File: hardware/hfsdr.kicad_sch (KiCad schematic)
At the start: 25 parts, among them J1 USB_C_Receptacle_USB2.0_16P, SW1 RST, SW2 BOOT0, U3 CH32V30xRxTx

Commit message: layout + some routing
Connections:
- net +3.3V: now also SW1.1 (A); no longer R4.1, SW1.2 (B)
- net SWDIO: now reaches U3.46 (SWDIO)
- net SWCLK: now reaches U3.49 (SWCLK)
- net at C20.2: now also R4.1, SW1.2 (B); no longer SW1.1 (A)
- no-connect marks 0 -> 4
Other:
- moved on the sheet: C20, SW1

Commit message: feat: routing
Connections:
- net DM renamed DN
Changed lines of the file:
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@@
 		)
 	)
-	(global_label "DM"
+	(global_label "DN"
 		(shape input)
 		(at 124.46 119.38 180)
@@
 		)
 		(property "Intersheetrefs" "${INTERSHEET_REFS}"
-			(at 118.7534 119.38 0)
+			(at 118.8743 119.38 0)
 			(effects
 				(font
@@
 		)
 	)
-	(global_label "DM"
+	(global_label "DN"
 		(shape input)
 		(at 241.3 43.18 180)
@@
 		)
 		(property "Intersheetrefs" "${INTERSHEET_REFS}"
-			(at 235.5934 43.18 0)
-			(effects
-				(font
+			(at 235.7143 43.18 0)
+			(effects
+				(font

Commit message: feat: most rules fixed?
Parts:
- removed H1: MountingHole_Pad, MountingHole:MountingHole_3.2mm_M3_Pad, symbol Mechanical:MountingHole_Pad
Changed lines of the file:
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@@
-	)
-	(symbol
-		(lib_id "Mechanical:MountingHole_Pad")
-		(at 222.25 76.2 0)
-		(unit 1)
-		(exclude_from_sim yes)
-		(in_bom no)
-		(on_board yes)
-		(dnp no)
-		(fields_autoplaced yes)
-		(property "Reference" "H1"
-			(at 224.79 73.6599 0)
-			(effects
-				(font
-					(size 1.27 1.27)
-				)
-				(justify left)
-			)
-		)
-		(property "Value" "MountingHole_Pad"
-			(at 224.79 76.1999 0)
-			(effects
-				(font
-					(size 1.27 1.27)
-				)
-				(justify left)
-			)
-		)
-		(property "Footprint" "MountingHole:MountingHole_3.2mm_M3_Pad"
-			(at 222.25 76.2 0)
-			(effects
-				(font
-					(size 1.27 1.27)
-				)
-				(hide yes)
-			)
-		)
-		(property "Datasheet" "~"
-			(at 222.25 76.2 0)
-			(effects
-				(font
-					(size 1.27 1.27)
-				)
-				(hide yes)
-			)
-		)
-		(property "Description" "Mounting Hole with connection"
-			(at 222.25 76.2 0)
-			(effects
-				(font
-					(size 1.27 1.27)
-				)
-				(hide yes)
-			)
-		)
-		(pin "1"
-		)
-		(instances
-			(project ""
-				(path "/a11445ed-c3bd-4d1c-a039-1c09b0dceab8"
-					(reference "H1")
-					(unit 1)
-				)
-			)
-		)
 	)
 	(symbol

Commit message: feat: hfsdr rough
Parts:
- added R12, R13, R14: 10k, Resistor_SMD:R_0805_2012Metric_Pad1.20x1.40mm_HandSolder, symbol Device:R
- added R15, R16: 4.7k, Resistor_SMD:R_0805_2012Metric_Pad1.20x1.40mm_HandSolder, symbol Device:R
- added SW4: EC12E2430803, easyeda2kicad:SW-TH_EC12EXXXX, symbol easyeda2kicad:EC12E2430803
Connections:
- net +3.3V: now also FPC1.17, R12.2, R13.2, R14.2, R15.2, R16.2
- net CS: now also U3.54 (PD2)
- net GND: now also SW4.C, SW4.D
- net RS: now also U3.53 (PC12)
- net RST: now also C20.2, FPC1.15, R4.1, SW1.2 (B)
- net SCL: now also FPC1.13, R15.1
- net SDA: now also FPC1.14, R16.1
- net ENC_B: now reaches U3.2 (PC13)
- net ENC_B: now also R14.1, SW4.B
- net ENC_A: now reaches U3.3 (PC14)
- net ENC_A: now also R13.1, SW4.A
- net ENC_BTN: now reaches U3.4 (PC15)
- net ENC_BTN: now also R12.1, SW4.E
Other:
- note added: "Touchscreen"

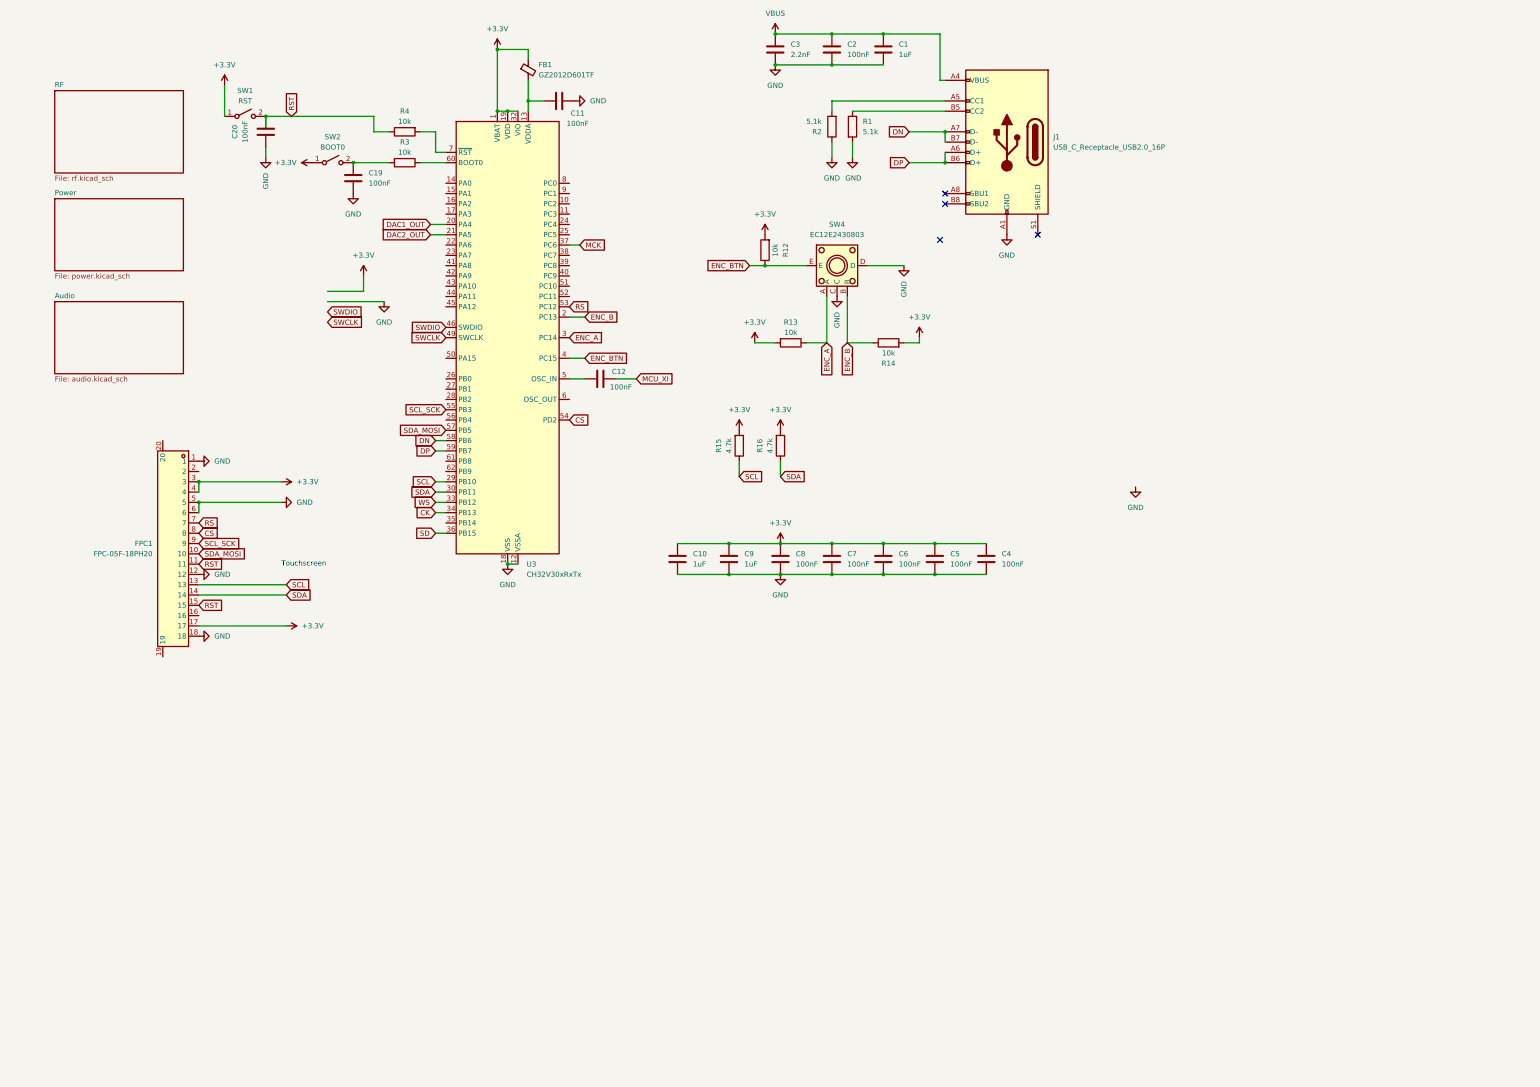
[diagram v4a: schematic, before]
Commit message: feat: add pads + fix adc chip footprint
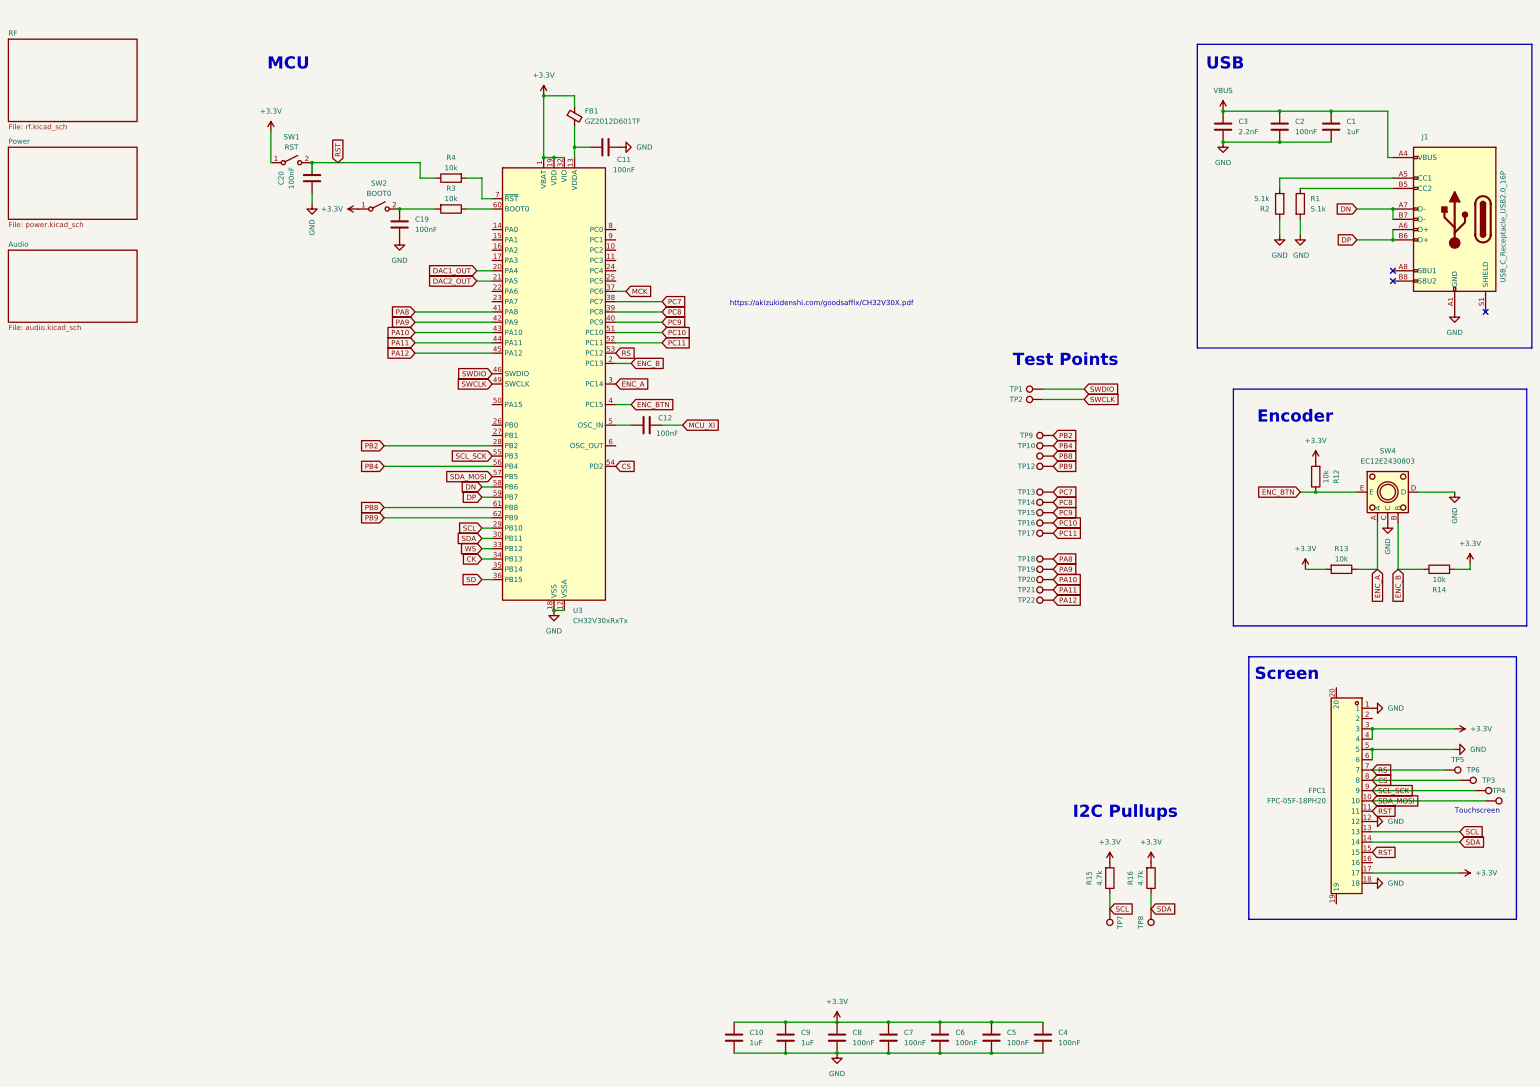
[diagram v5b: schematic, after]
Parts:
- added TP1, TP10, TP11, TP12, TP13, TP14, TP15, TP16, TP17, TP18, TP19, TP2, TP20, TP21, TP22, TP3, TP4, TP5, TP6, TP7, TP8, TP9: TestPoint, TestPoint:TestPoint_Pad_1.0x1.0mm, symbol Connector:TestPoint
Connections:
- net CS: now also TP6.1
- net RS: now also TP5.1
- net SCL: now also TP7.1
- net SCL_SCK: now also TP3.1
- net SDA: now also TP8.1
- net SDA_MOSI: now also TP4.1
- net SWCLK: now also TP2.1
- net SWDIO: now also TP1.1
- net PB2: now reaches U3.28 (PB2)
- net PB2: now also TP9.1
- net PC7: now reaches U3.38 (PC7)
- net PC7: now also TP13.1
- net PC8: now reaches U3.39 (PC8)
- net PC8: now also TP14.1
- net PC9: now reaches U3.40 (PC9)
- net PC9: now also TP15.1
- net PA8: now reaches U3.41 (PA8)
- net PA8: now also TP18.1
- net PA9: now reaches U3.42 (PA9)
- net PA9: now also TP19.1
- net PA10: now reaches U3.43 (PA10)
- net PA10: now also TP20.1
- net PA11: now reaches U3.44 (PA11)
- net PA11: now also TP21.1
- net PA12: now reaches U3.45 (PA12)
- net PA12: now also TP22.1
- net PC10: now reaches U3.51 (PC10)
- net PC10: now also TP16.1
- net PC11: now reaches U3.52 (PC11)
- net PC11: now also TP17.1
- net PB4: now reaches U3.56 (PB4)
- net PB4: now also TP10.1
- net PB8: now reaches U3.61 (PB8)
- net PB8: now also TP11.1
- net PB9: now reaches U3.62 (PB9)
- net PB9: now also TP12.1
- no-connect marks 4 -> 3
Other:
- note added: "Encoder"
- note added: "I2C Pullups"
- note added: "MCU"
- note added: "Screen"
- note added: "Test Points"
- note added: "USB"
- note added: "https://akizukidenshi.com/goodsaffix/CH32V30X.pdf"
- moved on the sheet: C1, C10, C11, C12, C19, C2, C20, C3, C4, C5, C6, C7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

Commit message: feat: add front LEDs
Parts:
- added D3, D4: LED, LED_SMD:LED_0603_1608Metric_Pad1.05x0.95mm_HandSolder, symbol Device:LED
- added R17, R18: 470, Resistor_SMD:R_0603_1608Metric_Pad0.98x0.95mm_HandSolder, symbol Device:R
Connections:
- net GND: now also R17.2, R18.2
- net LED1: now reaches U3.8 (PC0)
- net LED1: now also D3.2 (A)
- net LED2: now reaches U3.9 (PC1)
- net LED2: now also D4.2 (A)
- new net: D3.1 (K), R17.1
- new net: D4.1 (K), R18.1

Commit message: Production ready
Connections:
- net BATT_ADC: now reaches U3.24 (PC4)
- net VBUS_ADC: now reaches U3.25 (PC5)
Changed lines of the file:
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@@
+		)
+	)
+	(global_label "BATT_ADC"
+		(shape input)
+		(at 168.91 77.47 0)
+		(fields_autoplaced yes)
+		(effects
+			(font
+				(size 1.27 1.27)
+			)
+			(justify left)
+		)
+		(property "Intersheetrefs" "${INTERSHEET_REFS}"
+			(at 180.7852 77.47 0)
+			(effects
+				(font
+					(size 1.27 1.27)
+				)
+				(justify left)
+				(hide yes)
+			)
 		)
 	)
@@
 		)
 	)
+	(global_label "BATT_ADC"
+		(shape input)
+		(at 187.96 143.51 0)
+		(fields_autoplaced yes)
+		(effects
+			(font
+				(size 1.27 1.27)
+			)
+			(justify left)
+		)
+		(property "Intersheetrefs" "${INTERSHEET_REFS}"
+			(at 199.8352 143.51 0)
+			(effects
+				(font
+					(size 1.27 1.27)
+				)
+				(justify left)
+				(hide yes)
+			)
+		)
+	)
 	(global_label "LED1"
 		(shape input)
@@
 				(hide yes)
 			)
+		)
+	)
+	(global_label "VBUS_ADC"
+		(shape input)
+		(at 168.91 80.01 0)
+		(fields_autoplaced yes)
+		(effects
+			(font
+				(size 1.27 1.27)
+			)
+			(justify left)
+		)
+		(property "Intersheetrefs" "${INTERSHEET_REFS}"
+			(at 181.39 80.01 0)
+			(effects
+				(font
+					(size 1.27 1.27)
+				)
+				(justify left)
+				(hide yes)
+			)

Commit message: Update hardware
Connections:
- net +3.3V: now also C20.2, R4.1, SW1.2 (B); no longer SW1.1 (A)
- net GND: now also R3.2, SW1.1 (A)
- net PC10: now also FPC1.15
- net PC11: now also FPC1.11
- net at C19.1, SW2.2 (B): now also R3.1, U3.60 (BOOT0); no longer R3.2
- removed net RST: C20.2, FPC1.11, FPC1.15, R4.1, SW1.2 (B)
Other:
- moved on the sheet: R3, SW1
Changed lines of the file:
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@@
 	)
 	(junction
+		(at 128.27 62.23)
+		(diameter 0)
+		(color 0 0 0 0)
+	)
+	(junction
+		(at 115.57 62.23)
+		(diameter 0)
+		(color 0 0 0 0)
+	)
+	(junction
 		(at 236.22 270.51)
 		(diameter 0)
@@
 	)
 	(junction
-		(at 115.57 62.23)
+		(at 93.98 60.96)
 		(diameter 0)
 		(color 0 0 0 0)
@@
 	)
 	(junction
+		(at 191.77 92.71)
+		(diameter 0)
+		(color 0 0 0 0)
+	)
+	(junction
+		(at 115.57 69.85)
+		(diameter 0)
+		(color 0 0 0 0)
+	)
+	(junction
 		(at 318.77 45.72)
 		(diameter 0)
@@
 	)
 	(junction
+		(at 179.07 95.25)
+		(diameter 0)
+		(color 0 0 0 0)
+	)
+	(junction
 		(at 360.68 62.23)
 		(diameter 0)
@@
 	(wire
 		(pts
-			(xy 83.82 43.18) (xy 83.82 50.8)
+			(xy 119.38 87.63) (xy 138.43 87.63)
 		)
 		(stroke
@@
 	(wire
 		(pts
-			(xy 119.38 87.63) (xy 138.43 87.63)
+			(xy 318.77 38.1) (xy 332.74 38.1)
 		)
 		(stroke
@@
 	(wire
 		(pts
-			(xy 318.77 38.1) (xy 332.74 38.1)
+			(xy 332.74 54.61) (xy 360.68 54.61)
 		)
 		(stroke
@@
 	(wire
 		(pts
-			(xy 332.74 54.61) (xy 360.68 54.61)
+			(xy 339.09 151.13) (xy 344.17 151.13)
 		)
 		(stroke
@@
 	(wire
 		(pts
-			(xy 339.09 151.13) (xy 344.17 151.13)
+			(xy 135.89 130.81) (xy 138.43 130.81)
 		)
 		(stroke
@@
 	(wire
 		(pts
-			(xy 135.89 130.81) (xy 138.43 130.81)
+			(xy 360.68 67.31) (xy 360.68 69.85)
 		)
 		(stroke
@@
 	(wire
 		(pts
-			(xy 360.68 67.31) (xy 360.68 69.85)
+			(xy 82.55 60.96) (xy 93.98 60.96)
 		)
 		(stroke
@@
 	(wire
 		(pts
-			(xy 115.57 62.23) (xy 124.46 62.23)
+			(xy 179.07 95.25) (xy 168.91 95.25)
 		)
 		(stroke
@@
 	(wire
 		(pts
+			(xy 198.12 95.25) (xy 191.77 95.25)
+		)
+		(stroke
+			(width 0)
+			(type default)
+		)
+	)
+	(wire
+		(pts
+			(xy 191.77 92.71) (xy 168.91 92.71)
+		)
+		(stroke
+			(width 0)
+			(type default)
+		)
+	)
+	(wire
+		(pts
 			(xy 248.92 270.51) (xy 261.62 270.51)
 		)
@@
 	(wire
 		(pts
+			(xy 93.98 43.18) (xy 93.98 50.8)
+		)
+		(stroke
+			(width 0)
+			(type default)
+		)
+	)
+	(wire
+		(pts
+			(xy 115.57 69.85) (xy 128.27 69.85)
+		)
+		(stroke
+			(width 0)
+			(type default)
+		)
+	)
+	(wire
+		(pts
 			(xy 377.19 203.2) (xy 355.6 203.2)
 		)
@@
 	(wire
 		(pts
-			(xy 180.34 92.71) (xy 168.91 92.71)
+			(xy 82.55 50.8) (xy 93.98 50.8)
+		)
+		(stroke
+			(width 0)
+			(type default)
+		)
+	)
+	(wire
+		(pts
+			(xy 195.58 92.71) (xy 191.77 92.71)
 		)
 		(stroke
@@
 	(wire
 		(pts
+			(xy 191.77 95.25) (xy 191.77 92.71)
+		)
+		(stroke
+			(width 0)
+			(type default)
+		)
+	)
+	(wire
+		(pts
 			(xy 180.34 115.57) (xy 185.42 115.57)
 		)
@@
 	(wire
 		(pts
+			(xy 115.57 62.23) (xy 128.27 62.23)
+		)
+		(stroke
+			(width 0)
+			(type default)
+		)
+	)
+	(wire
+		(pts
 			(xy 180.34 87.63) (xy 168.91 87.63)
 		)
@@
 	(wire
 		(pts
+			(xy 182.88 97.79) (xy 179.07 97.79)
+		)
+		(stroke
+			(width 0)
+			(type default)
+		)
+	)
+	(wire
+		(pts
 			(xy 381 205.74) (xy 355.6 205.74)
 		)
@@
 	(wire
 		(pts
-			(xy 180.34 95.25) (xy 168.91 95.25)
+			(xy 180.34 95.25) (xy 179.07 95.25)
 		)
 		(stroke
@@
 	(wire
 		(pts
+			(xy 179.07 97.79) (xy 179.07 95.25)
+		)
+		(stroke
+			(width 0)
+			(type default)
+		)
+	)
+	(wire
+		(pts
 			(xy 158.75 41.91) (xy 158.75 46.99)
 		)
@@
 	(wire
 		(pts
-			(xy 132.08 62.23) (xy 138.43 62.23)
+			(xy 128.27 62.23) (xy 138.43 62.23)
 		)
 		(stroke
@@
 		)
 	)
-	(global_label "RST"
-		(shape input)
-		(at 100.33 50.8 90)
-		(fields_autoplaced yes)
-		(effects
-			(font
-				(size 1.27 1.27)
-			)
-			(justify left)
-		)
-		(property "Intersheetrefs" "${INTERSHEET_REFS}"
-			(at 100.33 44.3677 90)
-			(effects
-				(font
-					(size 1.27 1.27)
-				)
-				(justify left)
-				(hide yes)
-			)
-		)
-	)
 	(global_label "PB8"
 		(shape input)
@@
 		)
 	)
+	(global_label "RST"
+		(shape input)
+		(at 182.88 97.79 0)
+		(fields_autoplaced yes)
+		(effects
+			(font
+				(size 1.27 1.27)
+			)
+			(justify left)
+		)
+		(property "Intersheetrefs" "${INTERSHEET_REFS}"
+			(at 189.3123 97.79 0)
+			(effects
+				(font
+					(size 1.27 1.27)
+				)
+				(justify left)
+				(hide yes)
+			)
+		)
+	)
+	(global_label "TP_RST"
+		(shape input)
+		(at 198.12 95.25 0)
+		(fields_autoplaced yes)
+		(effects
+			(font
+				(size 1.27 1.27)
+			)
+			(justify left)
+		)
+		(property "Intersheetrefs" "${INTERSHEET_REFS}"
+			(at 207.7575 95.25 0)
+			(effects
+				(font
+					(size 1.27 1.27)
+				)
+				(justify left)
+				(hide yes)
+			)
+		)
+	)
 	(global_label "VBUS_ADC"
 		(shape input)
@@
 		)
 	)
-	(global_label "RST"
+	(global_label "TP_RST"
 		(shape input)
 		(at 355.6 220.98 0)
@@
 		)
 		(property "Intersheetrefs" "${INTERSHEET_REFS}"
-			(at 362.0323 220.98 0)
+			(at 365.2375 220.98 0)
 			(effects
 				(font
@@
 	(global_label "PC10"
 		(shape input)
-		(at 180.34 92.71 0)
+		(at 195.58 92.71 0)
 		(fields_autoplaced yes)
 		(effects
@@
 		)
 		(property "Intersheetrefs" "${INTERSHEET_REFS}"
-			(at 188.2842 92.71 0)
+			(at 203.5242 92.71 0)
 			(effects
 				(font
@@
 	(symbol
 		(lib_id "power:+3.3V")
-		(at 83.82 43.18 0)
+		(at 93.98 43.18 0)
 		(unit 1)
 		(exclude_from_sim no)
@@
 		(fields_autoplaced yes)
 		(property "Reference" "#PWR025"
-			(at 83.82 46.99 0)
+			(at 93.98 46.99 0)
 			(effects
 				(font
@@
 		)
 		(property "Value" "+3.3V"
-			(at 83.82 38.1 0)
+			(at 93.98 38.1 0)
 			(effects
 				(font
@@
 		)
 		(property "Footprint" ""
-			(at 83.82 43.18 0)
+			(at 93.98 43.18 0)
 			(effects
 				(font
@@
 		)
 		(property "Datasheet" ""
-			(at 83.82 43.18 0)
+			(at 93.98 43.18 0)
 			(effects
 				(font
@@
 		)
 		(property "Description" "Power symbol creates a global label with name \"+3.3V\""
-			(at 83.82 43.18 0)
+			(at 93.98 43.18 0)
 			(effects
 				(font
@@
 	(symbol
 		(lib_id "Switch:SW_SPST")
-		(at 88.9 50.8 0)
+		(at 82.55 55.88 270)
+		(mirror x)
 		(unit 1)
 		(exclude_from_sim no)
@@
 		(on_board yes)
 		(dnp no)
-		(fields_autoplaced yes)
 		(property "Reference" "SW1"
-			(at 88.9 44.45 0)
+			(at 81.28 54.6099 90)
 			(effects
 				(font
 					(size 1.27 1.27)
 				)
+				(justify right)
 			)
 		)
 		(property "Value" "RST"
-			(at 88.9 46.99 0)
+			(at 81.28 57.1499 90)
 			(effects
 				(font
 					(size 1.27 1.27)
 				)
+				(justify right)
 			)
 		)
 		(property "Footprint" "Button_Switch_SMD:SW_Push_1P1T_XKB_TS-1187A"
-			(at 88.9 50.8 0)
+			(at 82.55 55.88 0)
 			(effects
 				(font
@@
 		)
 		(property "Datasheet" "~"
-			(at 88.9 50.8 0)
+			(at 82.55 55.88 0)
 			(effects
 				(font
@@
 		)
 		(property "Description" "Single Pole Single Throw (SPST) switch"
-			(at 88.9 50.8 0)
+			(at 82.55 55.88 0)
 			(effects
 				(font
@@
 	(symbol
 		(lib_id "Device:R")
-		(at 128.27 62.23 270)
+		(at 128.27 66.04 0)
+		(mirror y)
 		(unit 1)
 		(exclude_from_sim no)
@@
 		(dnp no)
 		(property "Reference" "R3"
-			(at 128.27 57.15 90)
+			(at 132.08 67.31 0)
 			(effects
 				(font
@@
 		)
 		(property "Value" "10k"
-			(at 128.27 59.69 90)
+			(at 132.08 64.77 0)
 			(effects
 				(font
@@
 		)
 		(property "Footprint" "Resistor_SMD:R_0805_2012Metric_Pad1.20x1.40mm_HandSolder"
-			(at 128.27 60.452 90)
+			(at 130.048 66.04 90)
 			(effects
 				(font
@@
 		)
 		(property "Datasheet" "~"
-			(at 128.27 62.23 0)
+			(at 128.27 66.04 0)
 			(effects
 				(font
@@
 		)
 		(property "Description" "Resistor"
-			(at 128.27 62.23 0)
+			(at 128.27 66.04 0)
 			(effects
 				(font
